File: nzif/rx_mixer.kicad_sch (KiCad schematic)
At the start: 24 parts, among them U1 SN74CBT355CPW, U2 SN74CBT355CPW, U3 SN74CBT355CPW, U4 SN74CBT355CPW, U5 ADA4898-2, U6 ADA4898-2, U7 ADA4898-2, U8 ADA4898-2

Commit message: add supplies for switches on driver amp sheet
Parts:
- renumbered C1 to C101, C3 to C102, C2 to C103, C4 to C104, C5 to C105, C6 to C106, C7 to C107, C8 to C108, HC_0 to HC_101, HC_90 to HC_102, HC_45 to HC_103, HC_135 to HC_104, HC_180 to HC_105, HC_225 to HC_106, HC_270 to HC_107, HC_315 to HC_108, U1 to U107, U2 to U108, U3 to U112, U4 to U113
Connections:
- net -12V: no longer U5.4 (V-), U5.9 (EP), U6.4 (V-), U6.9 (EP), U7.4 (V-), U7.9 (EP), U8.4 (V-), U8.9 (EP)
- net 12V: no longer U5.8 (V+), U6.8 (V+), U7.8 (V+), U8.8 (V+)
- net BB_180: now also U7.1, U7.2 (-); no longer U7.6 (-), U7.7
- net BB_225: now also U6.1, U6.2 (-); no longer U6.6 (-), U6.7
- net BB_270: now also U5.2 (-); no longer U5.6 (-)
- net BB_315: now also U8.1, U8.2 (-); no longer U8.6 (-), U8.7
- net Baseband_180: now also U7.3 (+); no longer U7.5 (+)
- net Baseband_225: now also U6.3 (+); no longer U6.5 (+)
- net Baseband_270: now also U5.3 (+); no longer U5.5 (+)
- net Baseband_315: now also U8.3 (+); no longer U8.5 (+)

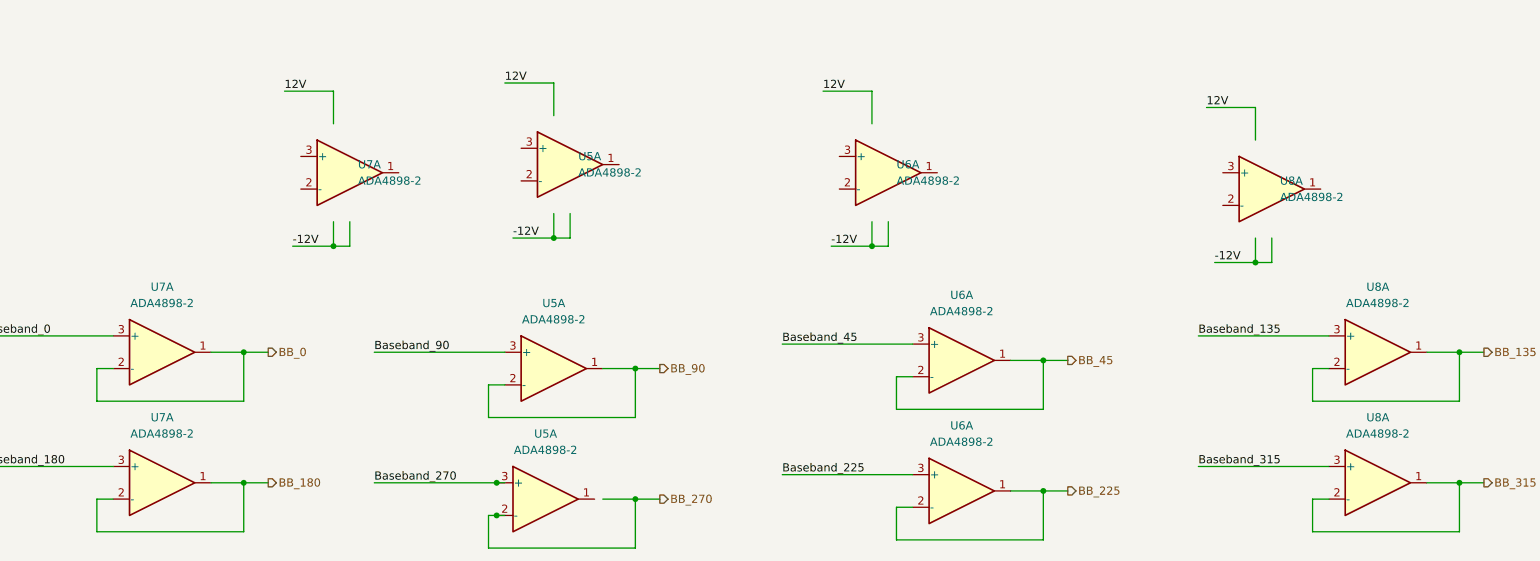
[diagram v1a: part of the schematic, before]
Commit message: Fix op amps to be correct units
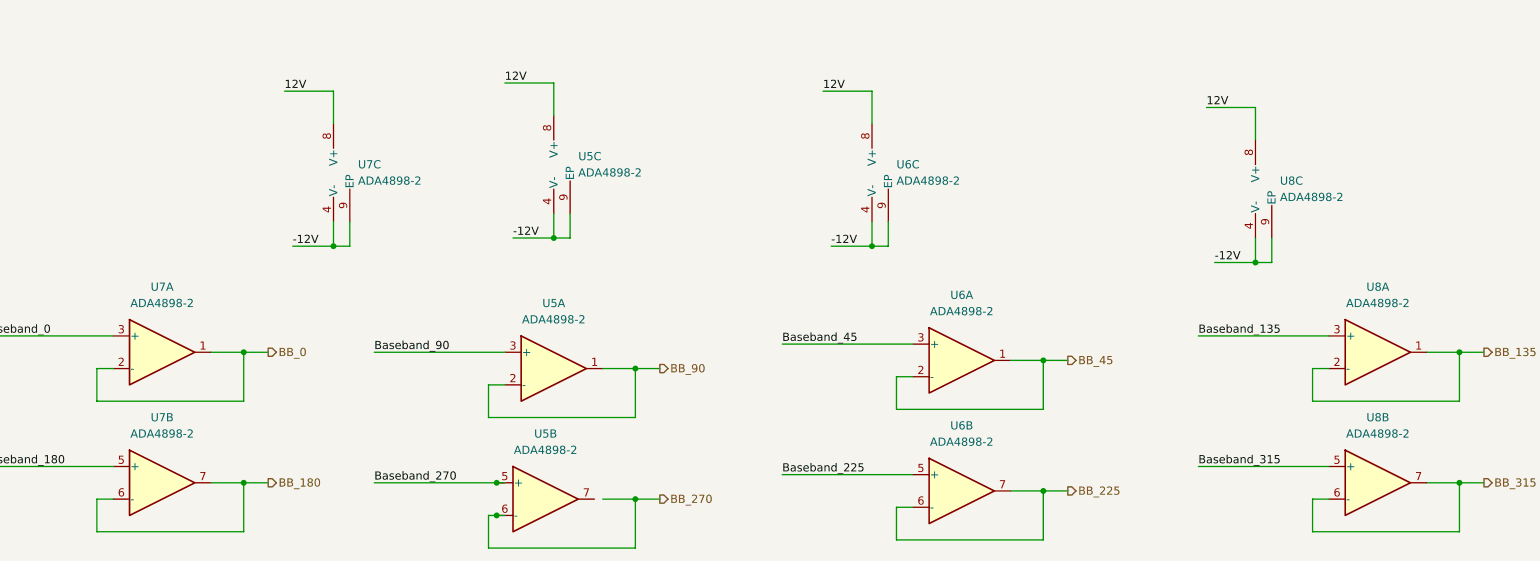
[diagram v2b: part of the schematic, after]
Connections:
- net -12V: now also U5.4 (V-), U5.9 (EP), U6.4 (V-), U6.9 (EP), U7.4 (V-), U7.9 (EP), U8.4 (V-), U8.9 (EP)
- net 12V: now also U5.8 (V+), U6.8 (V+), U7.8 (V+), U8.8 (V+)
- net BB_180: now also U7.6 (-), U7.7; no longer U7.1, U7.2 (-)
- net BB_225: now also U6.6 (-), U6.7; no longer U6.1, U6.2 (-)
- net BB_270: now also U5.6 (-); no longer U5.2 (-)
- net BB_315: now also U8.6 (-), U8.7; no longer U8.1, U8.2 (-)
- net Baseband_180: now also U7.5 (+); no longer U7.3 (+)
- net Baseband_225: now also U6.5 (+); no longer U6.3 (+)
- net Baseband_270: now also U5.5 (+); no longer U5.3 (+)
- net Baseband_315: now also U8.5 (+); no longer U8.3 (+)
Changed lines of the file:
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@@
 		(lib_id "Amplifier_Operational:ADA4898-2")
 		(at 120.65 251.46 0)
-		(unit 1)
+		(unit 2)
 		(exclude_from_sim yes)
 		(in_bom yes)
@@
 				(path "/fe42ca2f-2bb8-4d5a-9e84-807788ed632f/d923ed07-1122-4091-b99e-c24c264ea9d2"
 					(reference "U?")
-					(unit 1)
+					(unit 2)
 				)
 			)
@@
 		(lib_id "Amplifier_Operational:ADA4898-2")
 		(at 233.68 203.2 0)
-		(unit 1)
+		(unit 3)
 		(exclude_from_sim yes)
 		(in_bom yes)
@@
 				(path "/fe42ca2f-2bb8-4d5a-9e84-807788ed632f/d923ed07-1122-4091-b99e-c24c264ea9d2"
 					(reference "U?")
-					(unit 1)
+					(unit 3)
 				)
 			)
@@
 		(lib_id "Amplifier_Operational:ADA4898-2")
 		(at 90.17 200.66 0)
-		(unit 1)
+		(unit 3)
 		(exclude_from_sim yes)
 		(in_bom yes)
@@
 				(path "/fe42ca2f-2bb8-4d5a-9e84-807788ed632f/d923ed07-1122-4091-b99e-c24c264ea9d2"
 					(reference "U?")
-					(unit 1)
+					(unit 3)
 				)
 			)
@@
 		(lib_id "Amplifier_Operational:ADA4898-2")
 		(at 60.96 248.92 0)
-		(unit 1)
+		(unit 2)
 		(exclude_from_sim yes)
 		(in_bom yes)
@@
 				(path "/fe42ca2f-2bb8-4d5a-9e84-807788ed632f/d923ed07-1122-4091-b99e-c24c264ea9d2"
 					(reference "U?")
-					(unit 1)
+					(unit 2)
 				)
 			)
@@
 		(lib_id "Amplifier_Operational:ADA4898-2")
 		(at 124.46 199.39 0)
-		(unit 1)
+		(unit 3)
 		(exclude_from_sim yes)
 		(in_bom yes)
@@
 				(path "/fe42ca2f-2bb8-4d5a-9e84-807788ed632f/d923ed07-1122-4091-b99e-c24c264ea9d2"
 					(reference "U?")
-					(unit 1)
+					(unit 3)
 				)
 			)
@@
 		(lib_id "Amplifier_Operational:ADA4898-2")
 		(at 250.19 248.92 0)
-		(unit 1)
+		(unit 2)
 		(exclude_from_sim yes)
 		(in_bom yes)
@@
 				(path "/fe42ca2f-2bb8-4d5a-9e84-807788ed632f/d923ed07-1122-4091-b99e-c24c264ea9d2"
 					(reference "U?")
-					(unit 1)
+					(unit 2)
 				)
 			)
@@
 		(lib_id "Amplifier_Operational:ADA4898-2")
 		(at 185.42 250.19 0)
-		(unit 1)
+		(unit 2)
 		(exclude_from_sim yes)
 		(in_bom yes)
@@
 				(path "/fe42ca2f-2bb8-4d5a-9e84-807788ed632f/d923ed07-1122-4091-b99e-c24c264ea9d2"
 					(reference "U?")
-					(unit 1)
+					(unit 2)
 				)
 			)
@@
 		(lib_id "Amplifier_Operational:ADA4898-2")
 		(at 173.99 200.66 0)
-		(unit 1)
+		(unit 3)
 		(exclude_from_sim yes)
 		(in_bom yes)
@@
 				(path "/fe42ca2f-2bb8-4d5a-9e84-807788ed632f/d923ed07-1122-4091-b99e-c24c264ea9d2"
 					(reference "U?")
-					(unit 1)
-				)
-			)
+					(unit 3)
+				)
+			)

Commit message: updating footprints for rx mixer
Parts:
- C101, C102, C105, C106: footprint (none) -> Capacitor_SMD:C_0603_1608Metric_Pad1.08x0.95mm_HandSolder; Digikey Part # (none) -> 587-3258-1-ND
- C103, C104, C107, C108: footprint (none) -> Capacitor_SMD:C_0603_1608Metric_Pad1.08x0.95mm_HandSolder; Digikey Part # (none) -> 490-GCM31C5C1H104FA16LCT-ND
- HC_101, HC_102, HC_103, HC_104, HC_105, HC_106, HC_107, HC_108: footprint (none) -> Capacitor_SMD:C_0603_1608Metric_Pad1.08x0.95mm_HandSolder
- U107, U108, U112, U113: Digikey Part # (none) -> 296-SN74CBT3125CPWRTR-ND

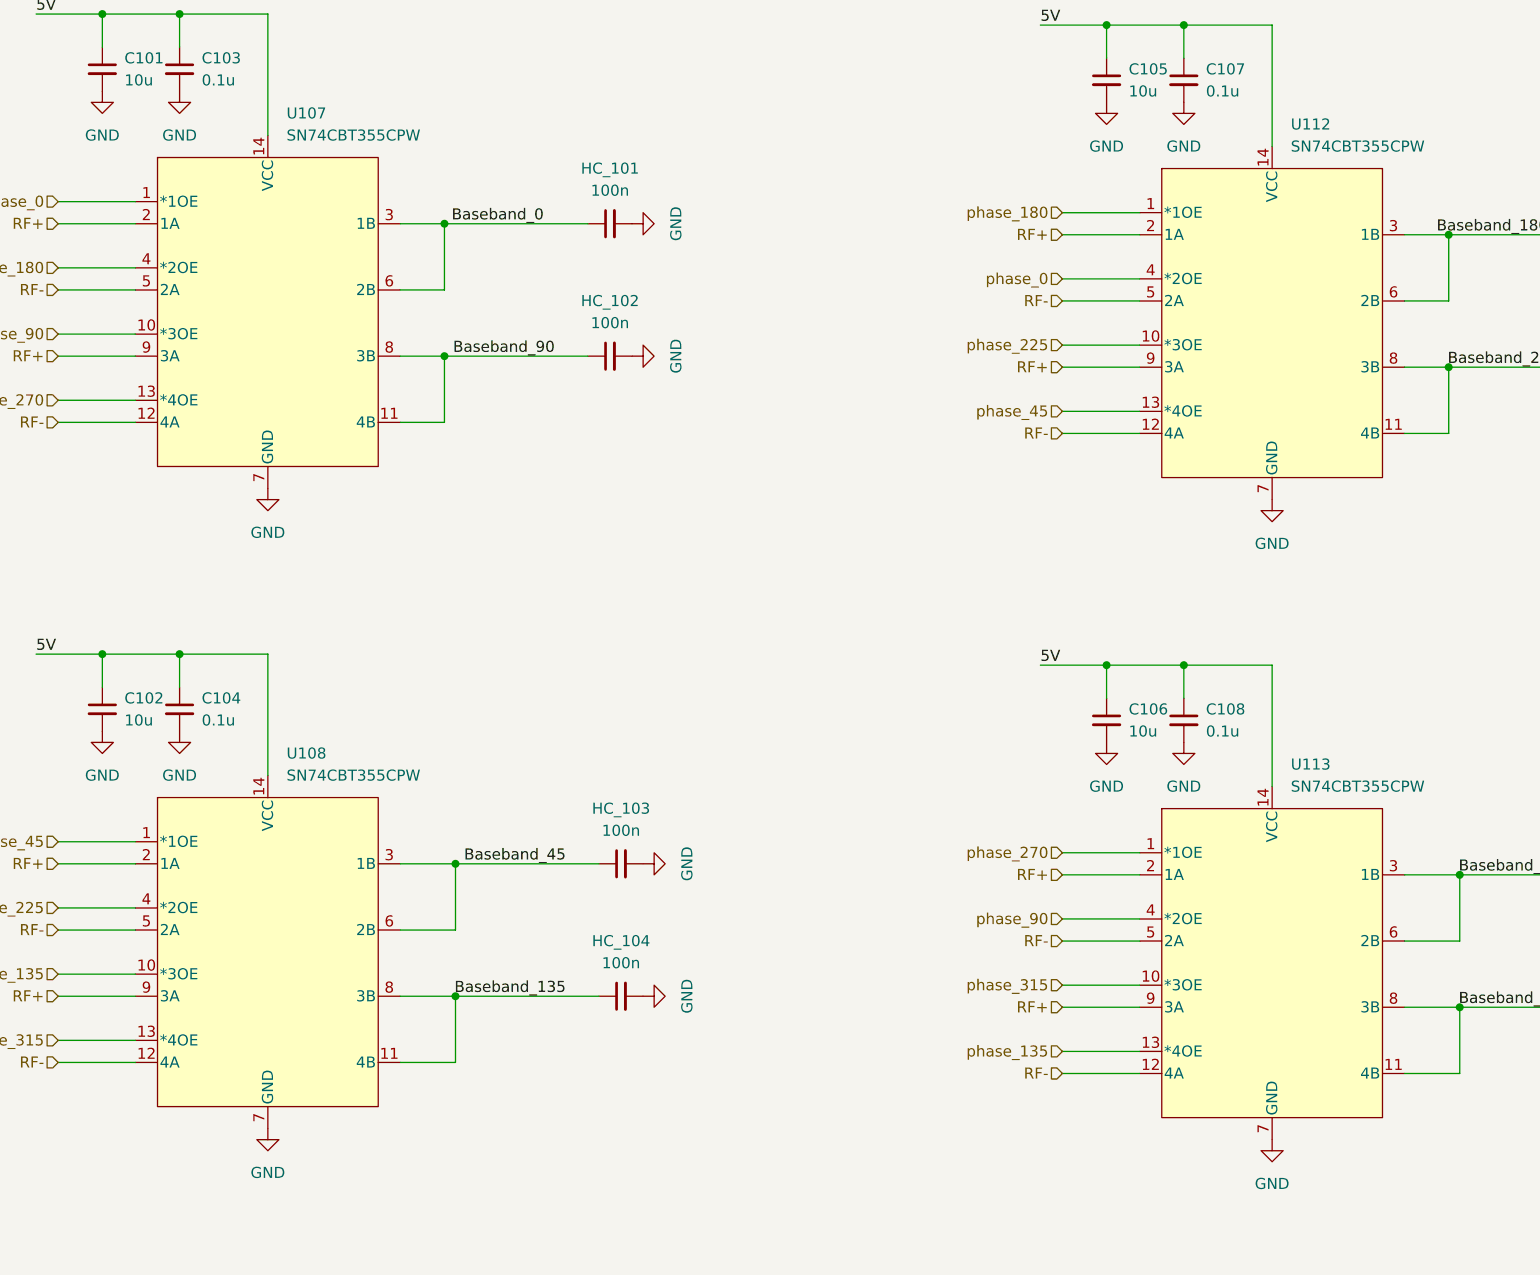
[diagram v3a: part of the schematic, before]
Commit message: sn74cbt3125c klc compliant
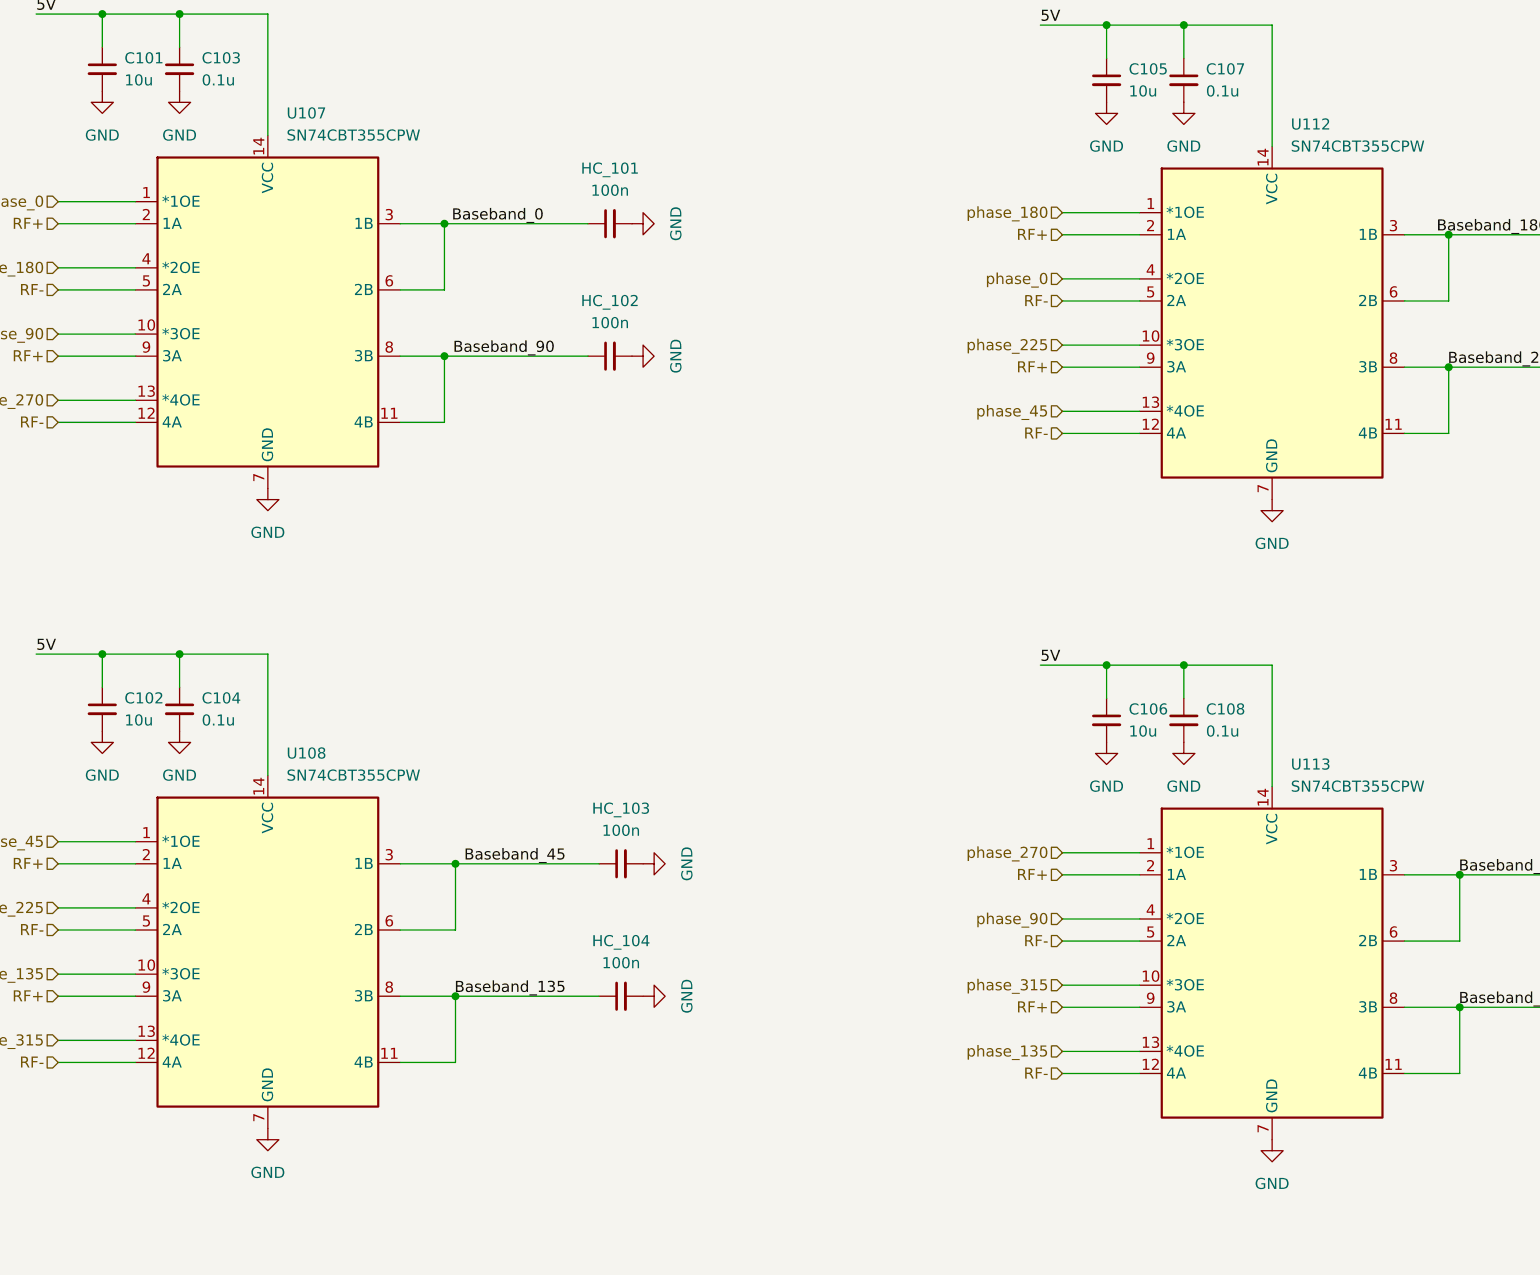
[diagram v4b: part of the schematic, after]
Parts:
- U107, U108, U112, U113: footprint nzif_footprints:PW14 -> Package_SO:TSSOP-14-1EP_4.4x5mm_P0.65mm
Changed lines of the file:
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@@
 			)
 		)
-		(property "Footprint" "nzif_footprints:PW14"
+		(property "Footprint" "Package_SO:TSSOP-14-1EP_4.4x5mm_P0.65mm"
 			(at 82.55 107.95 0)
 			(effects
@@
 			)
 		)
-		(property "Footprint" "nzif_footprints:PW14"
+		(property "Footprint" "Package_SO:TSSOP-14-1EP_4.4x5mm_P0.65mm"
 			(at 198.12 35.56 0)
 			(effects
@@
 			)
 		)
-		(property "Footprint" "nzif_footprints:PW14"
+		(property "Footprint" "Package_SO:TSSOP-14-1EP_4.4x5mm_P0.65mm"
 			(at 198.12 109.22 0)
 			(effects
@@
 			)
 		)
-		(property "Footprint" "nzif_footprints:PW14"
+		(property "Footprint" "Package_SO:TSSOP-14-1EP_4.4x5mm_P0.65mm"
 			(at 82.55 34.29 0)
 			(effects

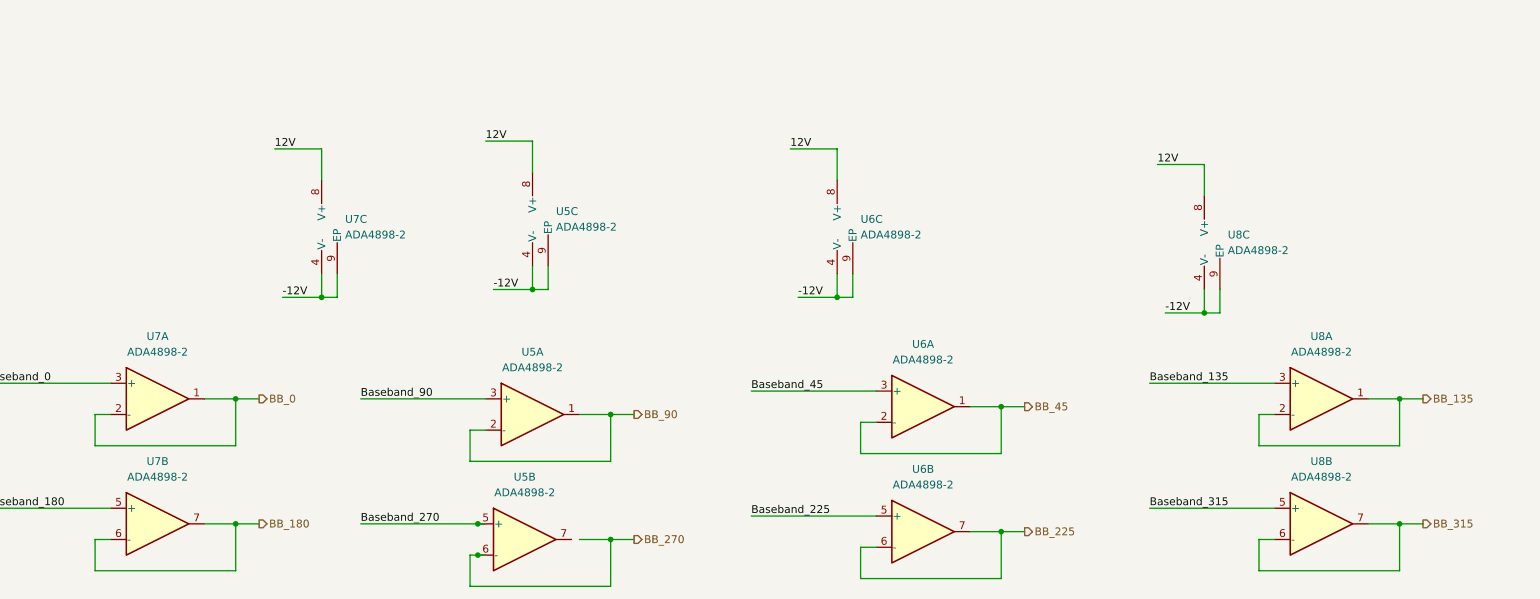
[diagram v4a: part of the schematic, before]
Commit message: ADA4625-2 added to RX Mixer
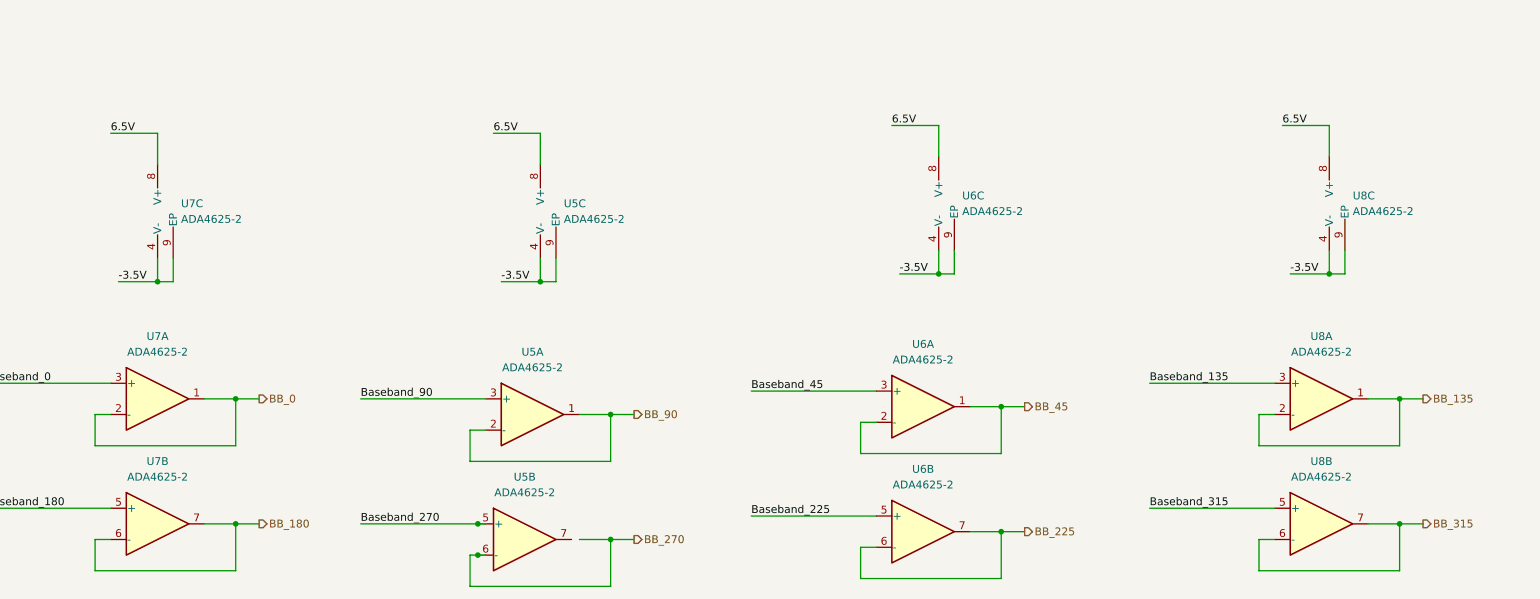
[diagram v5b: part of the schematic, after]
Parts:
- U5, U6, U7, U8: value ADA4898-2 -> ADA4625-2; footprint Package_SO:SOIC-8-1EP_3.9x4.9mm_P1.27mm_EP2.41x3.81mm -> Package_SO:SOIC-8-1EP_3.9x4.9mm_P1.27mm_EP2.29x3mm; symbol Amplifier_Operational:ADA4898-2 -> Amplifier_Operational:ADA4625-2ARDZ
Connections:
- net -12V renamed -3.5V
- net 12V renamed 6.5V
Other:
- moved on the sheet: U5C, U6C, U7C, U8C
